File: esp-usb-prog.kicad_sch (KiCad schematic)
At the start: 19 parts, among them J1 USB_B_Micro, Q10 BC817, Q9 BC817, U4 CH340T, Y1 Crystal_GND24_Small

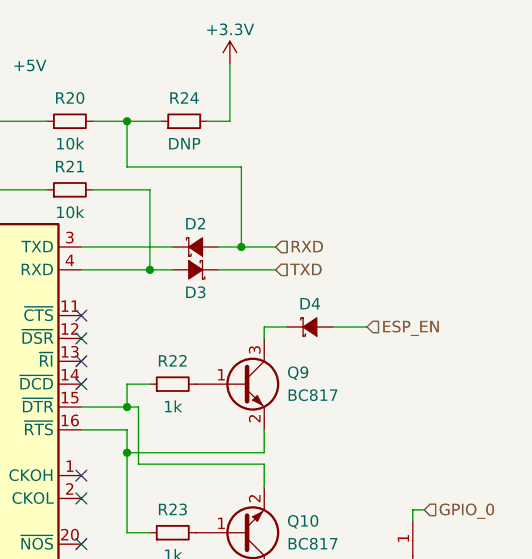
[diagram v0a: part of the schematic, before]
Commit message: Fixed FET footprints
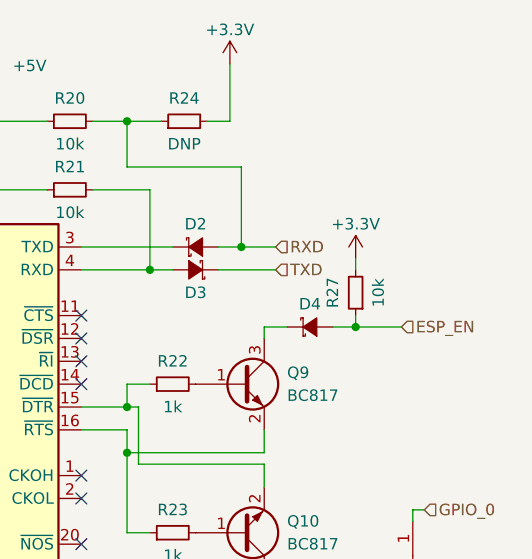
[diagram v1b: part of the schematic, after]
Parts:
- added R27: 10k, Resistor_SMD:R_0603_1608Metric, symbol wazombi:R_Small
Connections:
- net +3V3: now also R27.2
- net ESP_EN: now also R27.1
